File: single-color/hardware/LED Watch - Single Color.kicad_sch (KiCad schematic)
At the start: 197 parts, among them J1 LiPo, J1B LiPo, J2 UPDI pogo pads 1.27 mm (RESET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, M0 LED white 0402, M1 LED white 0402, M10 LED white 0402, M11 LED white 0402, M12 LED white 0402, M13 LED white 0402, M14 LED white 0402, M15 LED white 0402, M16 LED white 0402, M17 LED white 0402, M18 LED white 0402, M19 LED white 0402, M2 LED white 0402, M20 LED white 0402, M21 LED white 0402, M22 LED white 0402, M23 LED white 0402, M24 LED white 0402, M25 LED white 0402, M26 LED white 0402, M27 LED white 0402, M28 LED white 0402, M29 LED white 0402, M3 LED white 0402, M30 LED white 0402, M31 LED white 0402, M32 LED white 0402, M33 LED white 0402, M34 LED white 0402, M35 LED white 0402, M36 LED white 0402, M37 LED white 0402, M38 LED white 0402, M39 LED white 0402, M4 LED white 0402, M40 LED white 0402, M41 LED white 0402, M42 LED white 0402, M43 LED white 0402, M44 LED white 0402, M45 LED white 0402, M46 LED white 0402, M47 LED white 0402, M48 LED white 0402, M49 LED white 0402, M5 LED white 0402, M50 LED white 0402, M51 LED white 0402, M52 LED white 0402, M53 LED white 0402, M54 LED white 0402, M55 LED white 0402, M56 LED white 0402, M57 LED white 0402, M58 LED white 0402, M59 LED white 0402, M6 LED white 0402, M7 LED white 0402, M8 LED white 0402, M9 LED white 0402, SW1 SW_Push, SW2 SW_Push, U1 AVR128DB48-I/6LX, U2 LIS2DW12TR, U4 BQ25570RGRR, Y1 32.768kHz

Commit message: single-color: pre-order review; VOUT divider R55/R56 to 7.32M/4.22M (inside the datasheet's recommended range), BOM 26 lines; review and no-oscilloscope bring-up test documents
Co-Authored-By: Claude Sonnet 5.5 <noreply@anthropic.com>
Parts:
- R55: value 6.49M -> 7.32M
- R56: value 3.74M -> 4.22M

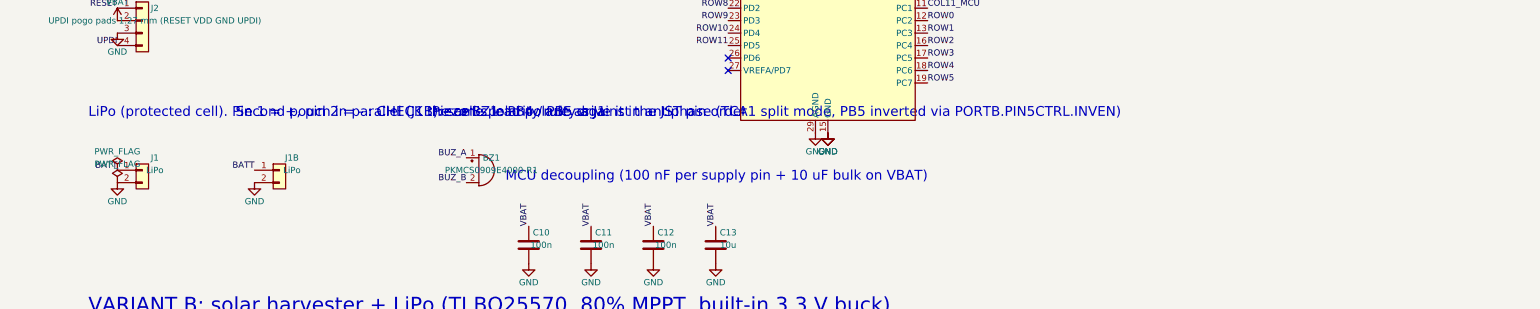
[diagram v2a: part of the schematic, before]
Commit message: single-color: battery plug polarity swapped to match TinyCircuits' wiring (pin 1 = GND, pin 2 = BATT), local back rework + silk marks, schematic/netlist/gerbers/docs updated; review section 7
Co-Authored-By: Claude Sonnet 5.5 <noreply@anthropic.com>
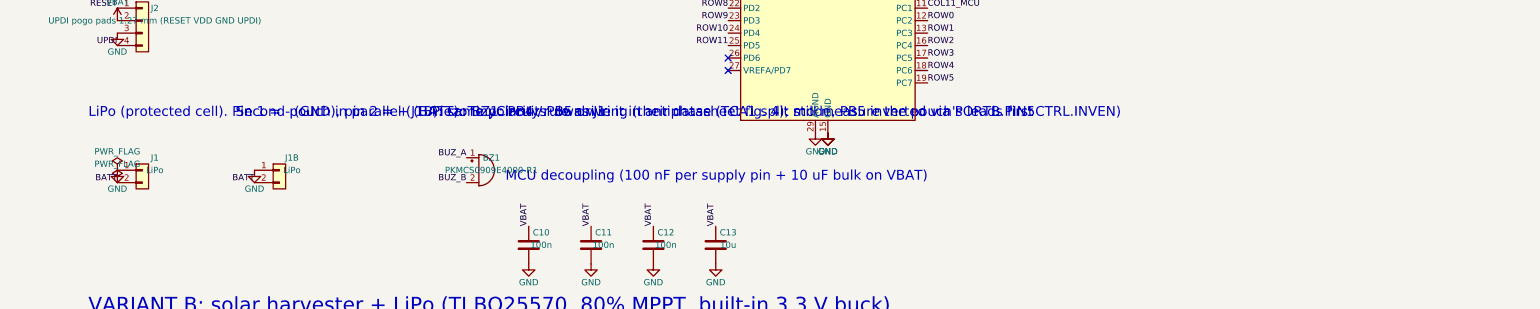
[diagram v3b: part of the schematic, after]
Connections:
- net BATT: now also J1.2 (Pin_2), J1B.2 (Pin_2); no longer J1.1 (Pin_1), J1B.1 (Pin_1)
- net GND: now also J1.1 (Pin_1), J1B.1 (Pin_1); no longer J1.2 (Pin_2), J1B.2 (Pin_2)
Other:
- note added: "LiPo (protected cell). Pin 1 = - (GND), pin 2 = + (BATT): TinyCircuits' own wiring (their datasheet fig. 4); still measure the pouch's leads first"
- note removed: "LiPo (protected cell). Pin 1 = +, pin 2 = - : CHECK the cell's lead polarity against the JST pin order"
